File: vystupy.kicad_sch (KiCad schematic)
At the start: 34 parts, among them J10 NTC 100k B3950, J11 SHT40 #2, J13 Tepelna pojistka, J5 Topeni 24V, J8 Ventilator 24V, J9 Odtah 24V, Q1 SiS434DN, Q2 AO3422, Q3 AOD4185, Q4 AO3422, SW1 Tlacitko

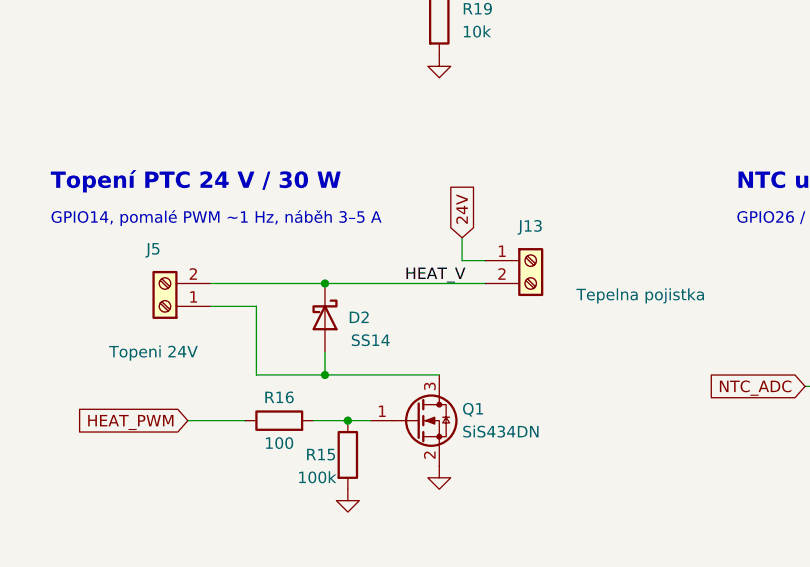
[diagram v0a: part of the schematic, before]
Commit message: Layout progress, VREG per reference, SI simulation, project notes
- Board: 70x100 mm outline, mounting holes, crystal, RP2350 decoupling,
  VREG copied from RP2350A Minimal R4 (zones, priorities, PGND track),
  RM2 placement and gSPI routing (CLK 16.5 mm, DATA 14.4 mm),
  RF keep-out rule area on all copper layers, test points TP12-TP15
- C4/C5/C6/R7 in 0402; C5/C6 use susicka:C_0402_1005Metric_RPi
  (0.56 mm pad gap so VREG_LX passes under the caps)
- simulace/wl_clk: KiCad ngspice model of WL_CLK (TLINE Z0 ~94 ohm,
  td ~96 ps) for transient and AC (Bode) analysis
- CLAUDE.md and Claude subagents (.claude/agents) moved into the PCB
  branch so the project context is available on other machines
- Ignore KiCad #auto_saved_files#

Co-Authored-By: Claude Opus 5.5 <noreply@anthropic.com>
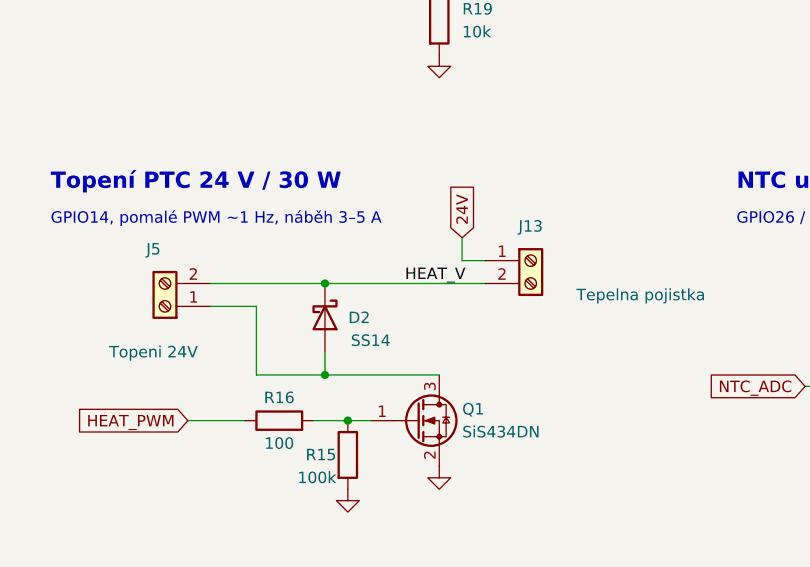
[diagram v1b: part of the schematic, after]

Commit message: Layout review fixes and JLCPCB fabrication outputs
- In2: GND pour over the whole board (priority 0) below the 3V3 zones
- Silkscreen: +/- marks of J5, J8, J9 moved out from under the terminal
  blocks; D4 and TP13 labels moved to visible spots
- TP12 moved away from the RM2 antenna keep-out, J4 shifted up,
  R20 220R so the D6 LED is visible at 3.3 V
- NTC (J10, R25, C26, TP19) excluded from this prototype board
- gerber/: fresh Gerber + Excellon export, JLCPCB zip, ordering notes
- CLAUDE.md, .claude/pamet.md: review results and decisions

Co-Authored-By: Claude Opus 5.5 <noreply@anthropic.com>
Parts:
- C26, J10, R25: now not fitted
- R20: value 1k -> 220
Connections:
- net 24V: now also J13.2 (Pin_2); no longer J13.1 (Pin_1)
- net HEAT_V: now also J13.1 (Pin_1); no longer J13.2 (Pin_2)
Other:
- moved on the sheet: J13
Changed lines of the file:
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@@
 	(wire
 		(pts
-			(xy 71.12 93.98) (xy 71.12 91.44)
-		)
-		(stroke
-			(width 0)
-			(type default)
-		)
-	)
-	(wire
-		(pts
 			(xy 114.3 53.34) (xy 114.3 50.8)
 		)
@@
 	(wire
 		(pts
-			(xy 142.24 110.49) (xy 139.7 110.49)
+			(xy 72.39 99.06) (xy 73.66 99.06)
 		)
 		(stroke
@@
 	(wire
 		(pts
-			(xy 43.18 99.06) (xy 48.26 99.06)
+			(xy 142.24 110.49) (xy 139.7 110.49)
 		)
 		(stroke
@@
 	(wire
 		(pts
-			(xy 73.66 93.98) (xy 71.12 93.98)
+			(xy 43.18 99.06) (xy 48.26 99.06)
 		)
 		(stroke
@@
 		)
 	)
-	(global_label "24V"
-		(shape input)
-		(at 71.12 91.44 90)
-		(fields_autoplaced yes)
-		(effects
-			(font
-				(size 1.27 1.27)
-			)
-			(justify left)
-		)
-		(property "Intersheetrefs" "${INTERSHEET_REFS}"
-			(at 71.12 91.44 0)
-			(effects
-				(font
-					(size 1.27 1.27)
-				)
-				(justify left)
-				(hide yes)
-			)
-		)
-	)
 	(global_label "SDA"
 		(shape bidirectional)
@@
 		)
 	)
+	(global_label "24V"
+		(shape input)
+		(at 72.39 99.06 270)
+		(fields_autoplaced yes)
+		(effects
+			(font
+				(size 1.27 1.27)
+			)
+			(justify right)
+		)
+		(property "Intersheetrefs" "${INTERSHEET_REFS}"
+			(at 72.39 105.5528 90)
+			(effects
+				(font
+					(size 1.27 1.27)
+				)
+				(justify right)
+				(hide yes)
+			)
+		)
+	)
 	(global_label "SCL0"
 		(shape bidirectional)
@@
 		(exclude_from_sim no)
 		(in_bom yes)
-		(on_board yes)
-		(dnp no)
+		(on_board no)
+		(dnp yes)
 		(property "Reference" "C26"
 			(at 132.08 110.49 0)
@@
 	(symbol
 		(lib_id "Connector:Screw_Terminal_01x02")
-		(at 78.74 93.98 0)
+		(at 78.74 96.52 0)
 		(unit 1)
 		(exclude_from_sim no)
@@
 		(dnp no)
 		(property "Reference" "J13"
-			(at 78.74 90.17 0)
+			(at 78.74 92.71 0)
 			(effects
 				(font
@@
 		)
 		(property "Value" "Tepelna pojistka"
-			(at 83.82 97.79 0)
+			(at 81.026 93.98 0)
 			(effects
 				(font
@@
 		)
 		(property "Footprint" "TerminalBlock_Phoenix:TerminalBlock_Phoenix_MKDS-1,5-2_1x02_P5.00mm_Horizontal"
-			(at 78.74 93.98 0)
+			(at 78.74 96.52 0)
 			(effects
 				(font
@@
 		)
 		(property "Datasheet" "~"
-			(at 78.74 93.98 0)
+			(at 78.74 96.52 0)
 			(effects
 				(font
@@
 		)
 		(property "Description" "Tepelná pojistka (TCO) na tělese topení, v sérii s topením"
-			(at 78.74 93.98 0)
+			(at 78.74 96.52 0)
 			(effects
 				(font
@@
 		(exclude_from_sim no)
 		(in_bom yes)
-		(on_board yes)
-		(dnp no)
+		(on_board no)
+		(dnp yes)
 		(property "Reference" "J10"
 			(at 149.86 105.41 0)
@@
 			)
 		)
-		(property "Value" "1k"
+		(property "Value" "220"
 			(at 182.88 53.34 90)
 			(effects
@@
 		(exclude_from_sim no)
 		(in_bom yes)
-		(on_board yes)
-		(dnp no)
+		(on_board no)
+		(dnp yes)
 		(property "Reference" "R25"
 			(at 121.92 100.33 0)
